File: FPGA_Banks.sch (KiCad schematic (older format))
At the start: 37 parts

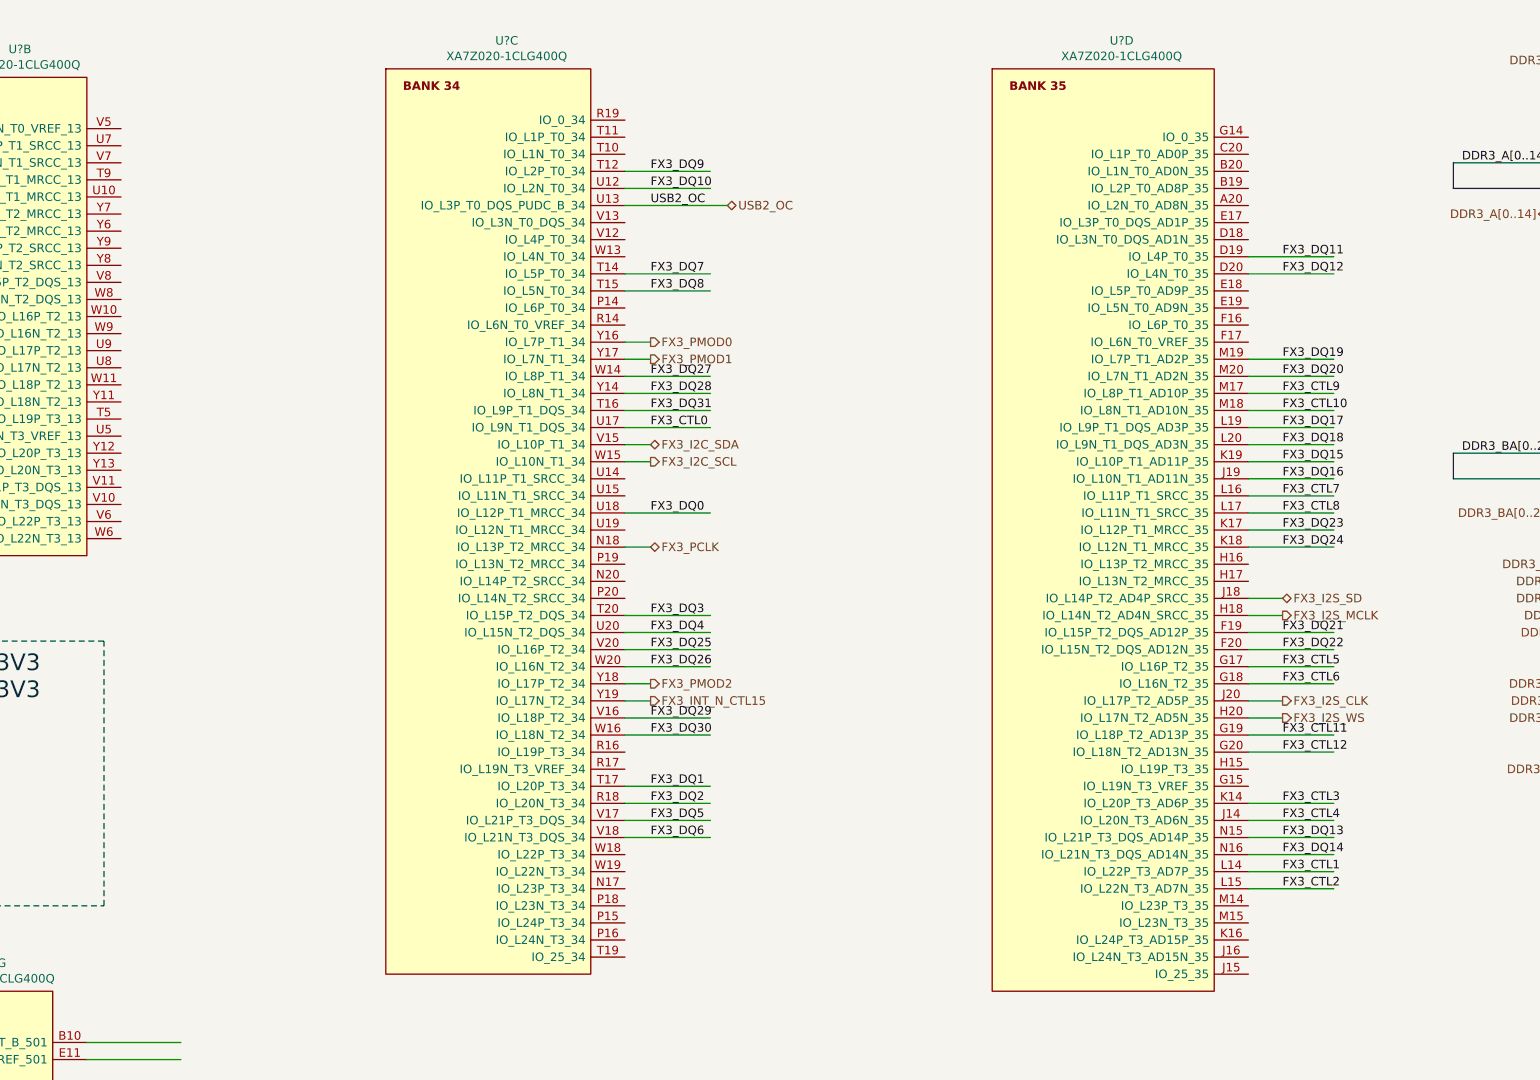
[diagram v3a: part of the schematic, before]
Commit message: Added ADC, DAC ,Clock pins to FPGA_Banks
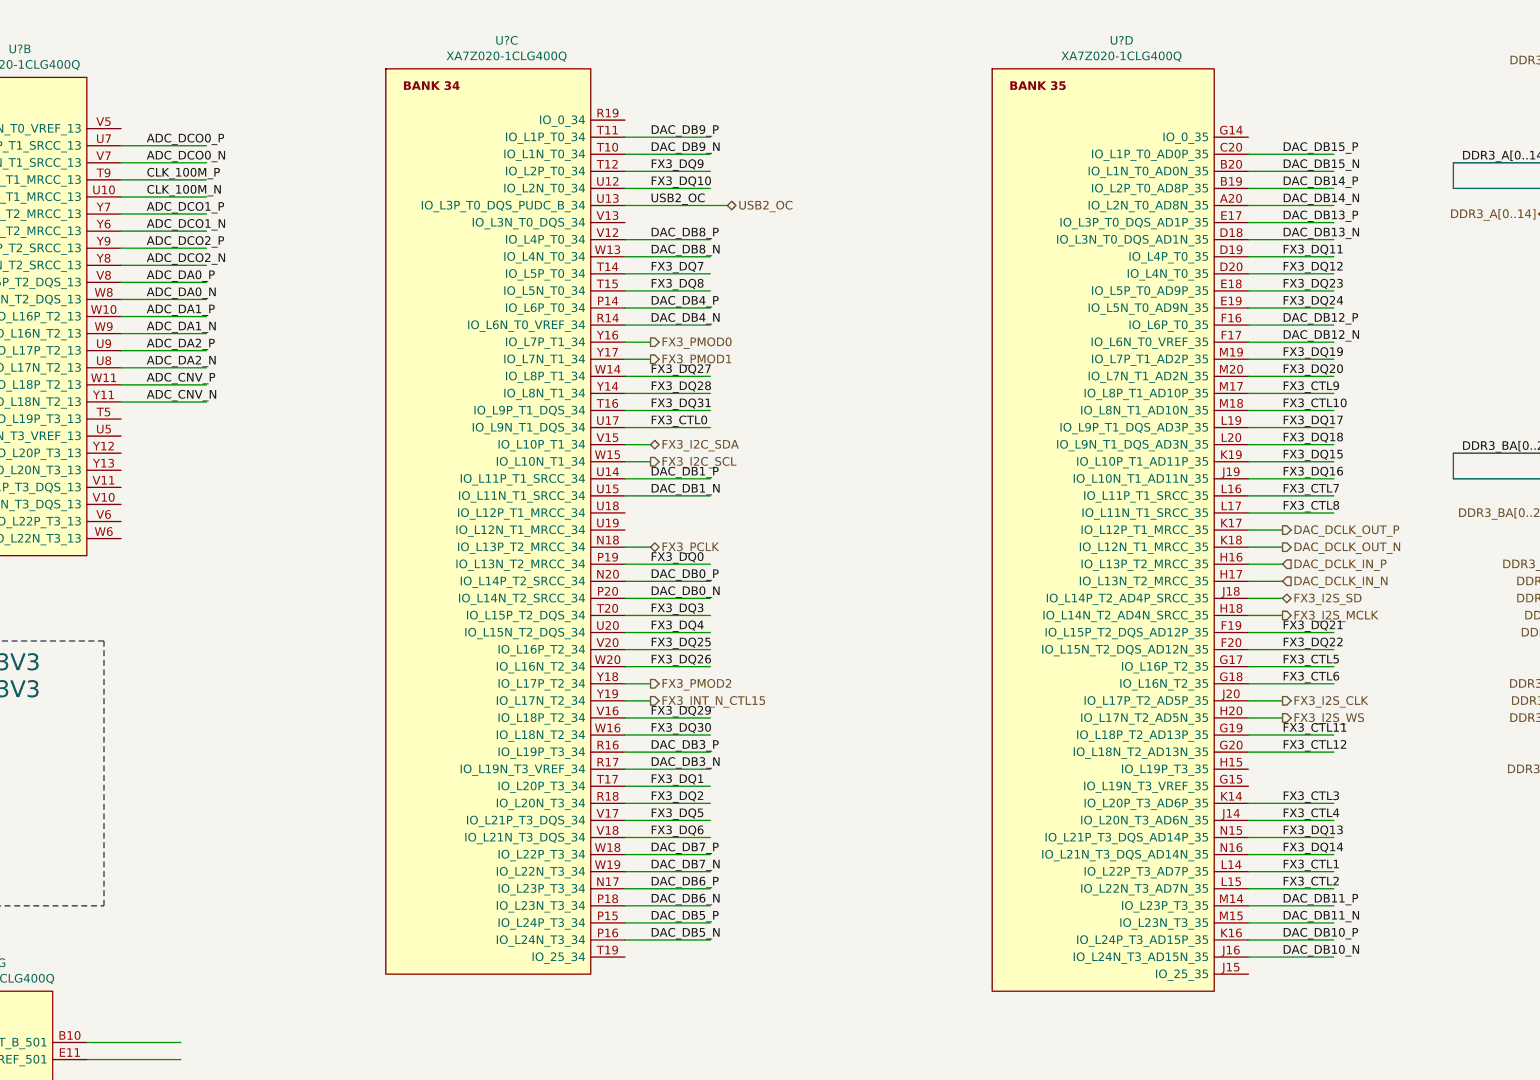
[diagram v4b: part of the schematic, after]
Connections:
- net labels added: ADC_CNV_N, ADC_CNV_P, ADC_DA0_N, ADC_DA0_P, ADC_DA1_N, ADC_DA1_P, ADC_DA2_N, ADC_DA2_P, ADC_DCO0_N, ADC_DCO0_P, ADC_DCO1_N, ADC_DCO1_P, ADC_DCO2_N, ADC_DCO2_P, CLK_100M_N, CLK_100M_P, DAC_DB0_N, DAC_DB0_P, DAC_DB10_N, DAC_DB10_P, DAC_DB11_N, DAC_DB11_P, DAC_DB12_N, DAC_DB12_P, DAC_DB13_N, DAC_DB13_P, DAC_DB14_N, DAC_DB14_P, DAC_DB15_N, DAC_DB15_P, DAC_DB1_N, DAC_DB1_P, DAC_DB3_N, DAC_DB3_P, DAC_DB4_N, DAC_DB4_P, DAC_DB5_N, DAC_DB5_P, DAC_DB6_N, DAC_DB6_P, DAC_DB7_N, DAC_DB7_P, DAC_DB8_N, DAC_DB8_P, DAC_DB9_N, DAC_DB9_P, DAC_DCLK_IN_N, DAC_DCLK_IN_P, DAC_DCLK_OUT_N, DAC_DCLK_OUT_P
- wire segments 303 -> 353
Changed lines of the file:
@@
 	2600 4450 950  4450
 Wire Wire Line
-	5650 3700 6150 3700
+	5650 4000 6150 4000
 Wire Wire Line
 	5650 5300 6150 5300
-Text Label 5800 3700 0    50   ~ 0
+Text Label 5800 4000 0    50   ~ 0
 FX3_DQ0
 Text Label 5800 5300 0    50   ~ 0
@@
 Text Label 5800 1800 0    50   ~ 0
 FX3_DQ10
-Text Label 9500 2200 0    50   ~ 0
-FX3_DQ11
-Text Label 9500 2300 0    50   ~ 0
-FX3_DQ12
 Text Label 9500 5600 0    50   ~ 0
 FX3_DQ13
@@
 Text Label 9500 4500 0    50   ~ 0
 FX3_DQ22
-Text Label 9500 3800 0    50   ~ 0
-FX3_DQ23
-Text Label 9500 3900 0    50   ~ 0
-FX3_DQ24
 Text Label 5800 4500 0    50   ~ 0
 FX3_DQ25
@@
 	5650 1700 6150 1700
 Wire Wire Line
-	9300 2300 9800 2300
-Wire Wire Line
-	9300 2200 9800 2200
-Wire Wire Line
 	9300 2800 9800 2800
 Wire Wire Line
@@
 Wire Wire Line
 	9300 3500 9800 3500
-Wire Wire Line
-	9300 3800 9800 3800
-Wire Wire Line
-	9300 3900 9800 3900
 Wire Wire Line
 	9300 4400 9800 4400
@@
 Text Label 9500 3600 0    50   ~ 0
 FX3_CTL7
-Text Label 9500 3700 0    50   ~ 0
-FX3_CTL8
 Text Label 9500 3000 0    50   ~ 0
 FX3_CTL9
@@
 Wire Wire Line
 	6250 1900 5650 1900
+Wire Wire Line
+	9300 4000 9500 4000
+Text Label 9500 3700 0    50   ~ 0
+FX3_CTL8
+Wire Wire Line
+	9300 4100 9500 4100
+Text HLabel 9500 3800 2    50   Output ~ 0
+DAC_DCLK_OUT_P
+Text HLabel 9500 3900 2    50   Output ~ 0
+DAC_DCLK_OUT_N
+Wire Wire Line
+	9500 3800 9300 3800
+Wire Wire Line
+	9500 3900 9300 3900
+Text HLabel 9500 4000 2    50   Input ~ 0
+DAC_DCLK_IN_P
+Text HLabel 9500 4100 2    50   Input ~ 0
+DAC_DCLK_IN_N
+Text Label 9500 1600 0    50   ~ 0
+DAC_DB15_P
+Text Label 9500 1700 0    50   ~ 0
+DAC_DB15_N
+Wire Wire Line
+	9300 2500 9800 2500
+Wire Wire Line
+	9300 2400 9800 2400
+Wire Wire Line
+	9300 2300 9800 2300
+Wire Wire Line
+	9300 2200 9800 2200
+Text Label 9500 2500 0    50   ~ 0
+FX3_DQ24
+Text Label 9500 2400 0    50   ~ 0
+FX3_DQ23
+Text Label 9500 2300 0    50   ~ 0
+FX3_DQ12
+Text Label 9500 2200 0    50   ~ 0
+FX3_DQ11
+Wire Wire Line
+	9300 1600 9800 1600
+Wire Wire Line
+	9300 1700 9800 1700
+Text Label 9500 1800 0    50   ~ 0
+DAC_DB14_P
+Text Label 9500 1900 0    50   ~ 0
+DAC_DB14_N
+Wire Wire Line
+	9300 1800 9800 1800
+Wire Wire Line
+	9300 1900 9800 1900
+Text Label 9500 2000 0    50   ~ 0
+DAC_DB13_P
+Text Label 9500 2100 0    50   ~ 0
+DAC_DB13_N
+Wire Wire Line
+	9300 2000 9800 2000
+Wire Wire Line
+	9300 2100 9800 2100
+Text Label 9500 2600 0    50   ~ 0
+DAC_DB12_P
+Text Label 9500 2700 0    50   ~ 0
+DAC_DB12_N
+Wire Wire Line
+	9300 2600 9800 2600
+Wire Wire Line
+	9300 2700 9800 2700
+Text Label 9500 6000 0    50   ~ 0
+DAC_DB11_P
+Text Label 9500 6100 0    50   ~ 0
+DAC_DB11_N
+Wire Wire Line
+	9300 6000 9800 6000
+Wire Wire Line
+	9300 6100 9800 6100
+Text Label 9500 6200 0    50   ~ 0
+DAC_DB10_P
+Text Label 9500 6300 0    50   ~ 0
+DAC_DB10_N
+Wire Wire Line
+	9300 6200 9800 6200
+Wire Wire Line
+	9300 6300 9800 6300
+Text Label 5800 1500 0    50   ~ 0
+DAC_DB9_P
+Text Label 5800 1600 0    50   ~ 0
+DAC_DB9_N
+Wire Wire Line
+	5650 1500 6150 1500
+Wire Wire Line
+	5650 1600 6150 1600
+Text Label 5800 2100 0    50   ~ 0
+DAC_DB8_P
+Text Label 5800 2200 0    50   ~ 0
+DAC_DB8_N
+Wire Wire Line
+	5650 2100 6150 2100
+Wire Wire Line
+	5650 2200 6150 2200
+Text Label 5800 5700 0    50   ~ 0
+DAC_DB7_P
+Text Label 5800 5800 0    50   ~ 0
+DAC_DB7_N
+Wire Wire Line
+	5650 5700 6150 5700
+Wire Wire Line
+	5650 5800 6150 5800
+Text Label 5800 5900 0    50   ~ 0
+DAC_DB6_P
+Text Label 5800 6000 0    50   ~ 0
+DAC_DB6_N
+Wire Wire Line
+	5650 5900 6150 5900
+Wire Wire Line
+	5650 6000 6150 6000
+Text Label 5800 6100 0    50   ~ 0
+DAC_DB5_P
+Text Label 5800 6200 0    50   ~ 0
+DAC_DB5_N
+Wire Wire Line
+	5650 6100 6150 6100
+Wire Wire Line
+	5650 6200 6150 6200
+Text Label 5800 2500 0    50   ~ 0
+DAC_DB4_P
+Text Label 5800 2600 0    50   ~ 0
+DAC_DB4_N
+Wire Wire Line
+	5650 2500 6150 2500
+Wire Wire Line
+	5650 2600 6150 2600
+Text Label 5800 5100 0    50   ~ 0
+DAC_DB3_P
+Text Label 5800 5200 0    50   ~ 0
+DAC_DB3_N
+Wire Wire Line
+	5650 5100 6150 5100
+Wire Wire Line
+	5650 5200 6150 5200
+Text Label 5800 3500 0    50   ~ 0
+DAC_DB1_P
+Text Label 5800 3600 0    50   ~ 0
+DAC_DB1_N
+Wire Wire Line
+	5650 3500 6150 3500
+Wire Wire Line
+	5650 3600 6150 3600
+Text Label 5800 4100 0    50   ~ 0
+DAC_DB0_P
+Text Label 5800 4200 0    50   ~ 0
+DAC_DB0_N
+Wire Wire Line
+	5650 4100 6150 4100
+Wire Wire Line
+	5650 4200 6150 4200
+Text Label 2850 2950 0    50   ~ 0
+ADC_CNV_P
+Text Label 2850 3050 0    50   ~ 0
+ADC_CNV_N
+Wire Wire Line
+	2700 2950 3200 2950
+Wire Wire Line
+	2700 3050 3200 3050
+Text Label 2850 1550 0    50   ~ 0
+ADC_DCO0_P
+Text Label 2850 1650 0    50   ~ 0
+ADC_DCO0_N
+Wire Wire Line
+	2700 1550 3200 1550
+Wire Wire Line
+	2700 1650 3200 1650
+Text Label 2850 1950 0    50   ~ 0
+ADC_DCO1_P
+Text Label 2850 2050 0    50   ~ 0
+ADC_DCO1_N
+Wire Wire Line
+	2700 1950 3200 1950
+Wire Wire Line
+	2700 2050 3200 2050
+Text Label 2850 2150 0    50   ~ 0
+ADC_DCO2_P
+Text Label 2850 2250 0    50   ~ 0
+ADC_DCO2_N
+Wire Wire Line
+	2700 2150 3200 2150
+Wire Wire Line
+	2700 2250 3200 2250
+Text Label 2850 2350 0    50   ~ 0
+ADC_DA0_P
+Text Label 2850 2450 0    50   ~ 0
+ADC_DA0_N
+Wire Wire Line
+	2700 2350 3200 2350
+Wire Wire Line
+	2700 2450 3200 2450
+Text Label 2850 2550 0    50   ~ 0
+ADC_DA1_P
+Text Label 2850 2650 0    50   ~ 0
+ADC_DA1_N
+Wire Wire Line
+	2700 2550 3200 2550
+Wire Wire Line
+	2700 2650 3200 2650
+Text Label 2850 2750 0    50   ~ 0
+ADC_DA2_P
+Text Label 2850 2850 0    50   ~ 0
+ADC_DA2_N
+Wire Wire Line
+	2700 2750 3200 2750
+Wire Wire Line
+	2700 2850 3200 2850
+Text Label 2850 1750 0    50   ~ 0
+CLK_100M_P
+Text Label 2850 1850 0    50   ~ 0
+CLK_100M_N
+Wire Wire Line
+	2700 1750 3200 1750
+Wire Wire Line
+	2700 1850 3200 1850
 Wire Bus Line
 	11200 3350 11200 3600

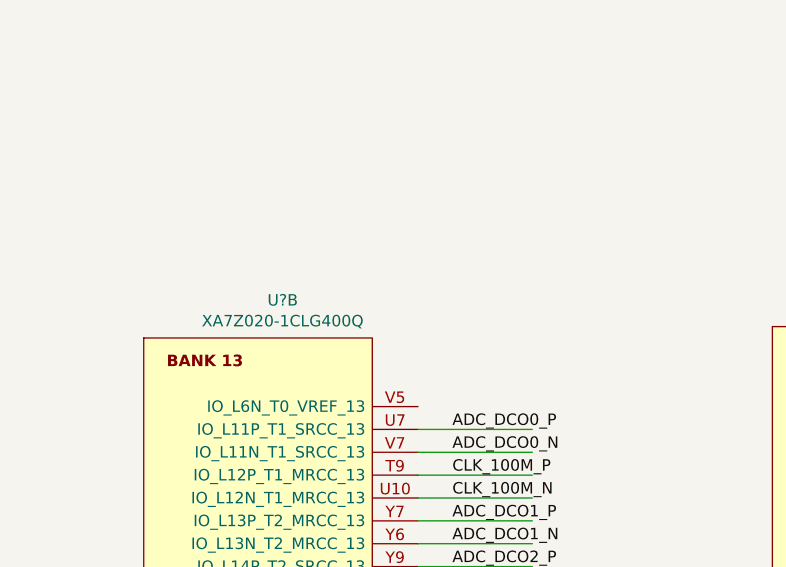
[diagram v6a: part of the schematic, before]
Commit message: Added Fast DAC schematic
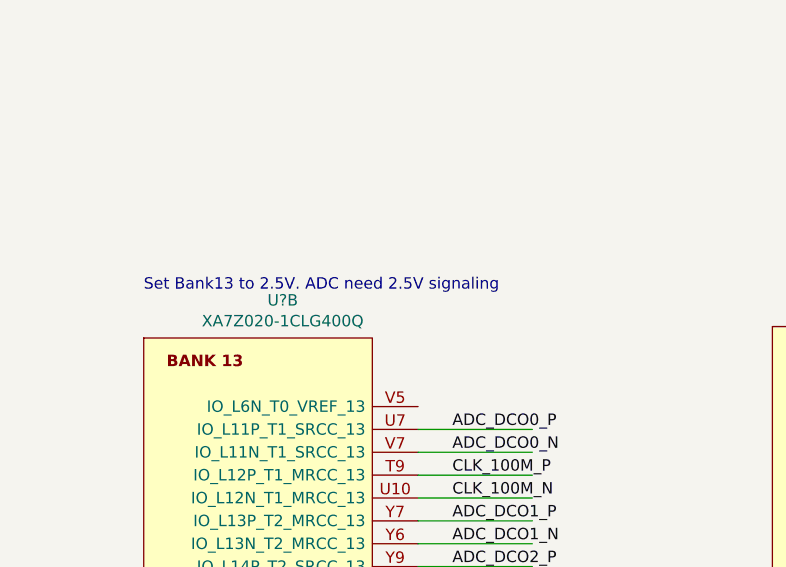
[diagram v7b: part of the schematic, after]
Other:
- note added: "Set Bank13 to 2.5V. ADC need 2.5V signaling"
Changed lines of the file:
@@
 Wire Bus Line
 	12250 7900 12250 9600
+Text Notes 1500 950  0    50   ~ 0
+Set Bank13 to 2.5V. ADC need 2.5V signaling
 $EndSCHEMATC
